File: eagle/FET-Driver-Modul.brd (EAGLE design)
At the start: 60 x 60 mm, 19 parts, among them X1 MKDSN1,5/3-5,08

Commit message: Lots of schema and board changes
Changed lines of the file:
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@@
 <wire x1="43.18" y1="52.07" x2="44.45" y2="54.61" width="1.016" layer="16"/>
 <contactref element="JP5" pad="1"/>
-<wire x1="25.4" y1="14.605" x2="26.67" y2="8.89" width="1.016" layer="16"/>
-<wire x1="26.67" y1="8.89" x2="34.29" y2="1.27" width="1.016" layer="16"/>
+<wire x1="25.4" y1="14.605" x2="25.4" y2="10.16" width="1.016" layer="16"/>
+<wire x1="25.4" y1="10.16" x2="34.29" y2="1.27" width="1.016" layer="16"/>
 <wire x1="34.29" y1="1.27" x2="47.625" y2="1.27" width="1.016" layer="16"/>
 <wire x1="47.625" y1="1.27" x2="49.53" y2="3.175" width="1.016" layer="16"/>

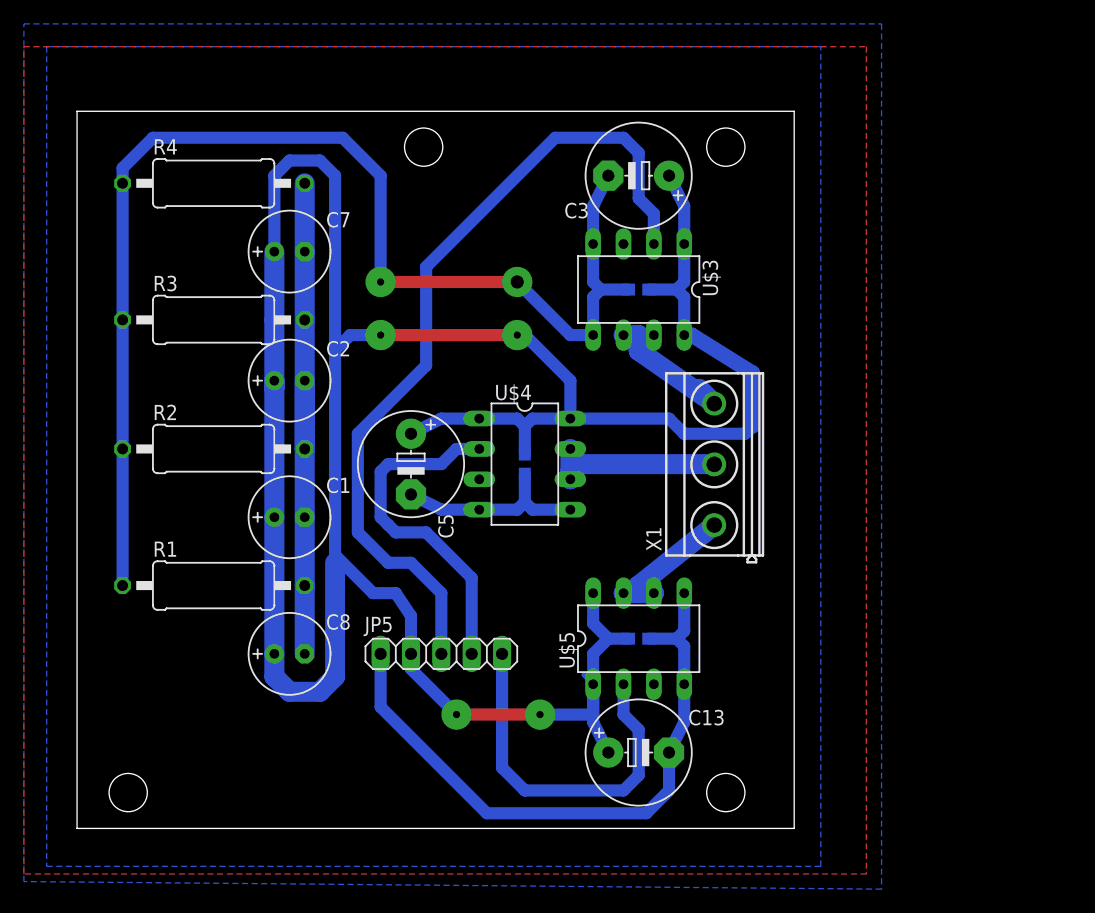
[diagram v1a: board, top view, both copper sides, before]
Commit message: Adjusted drill positions, little size corrections, new pin header
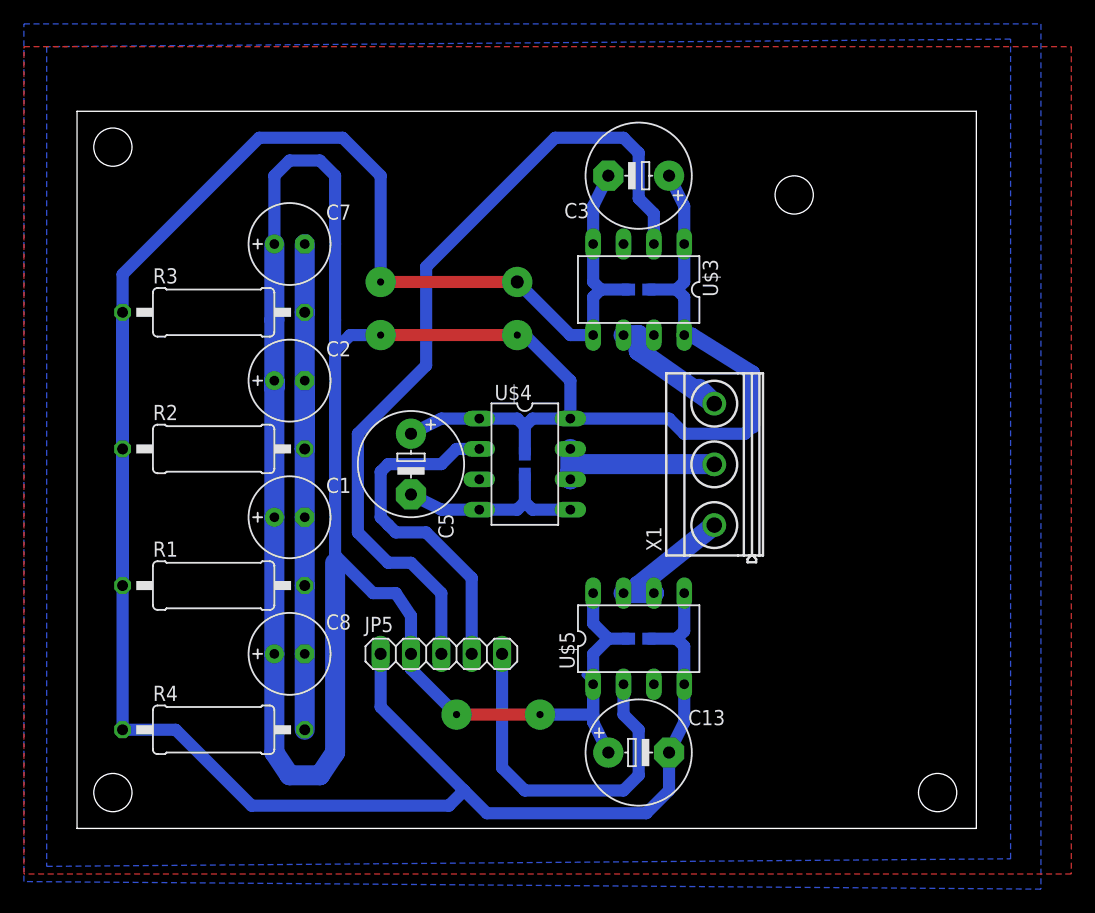
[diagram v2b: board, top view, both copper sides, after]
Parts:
- moved R4 45.7 mm to (11.4, 8.26)
- moved C7 0.64 mm to (17.8, 48.9)
- moved R3 0.63 mm to (11.4, 43.2)
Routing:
- net GND: track 156.6 -> 218.0 mm
- net N$2: track 231.7 -> 245.4 mm
- net N$4: track 50.8 -> 52.1 mm
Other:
- board size 60 x 60 mm -> 75.2 x 60 mm
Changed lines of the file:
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@@
 <board>
 <plain>
-<wire x1="0" y1="0" x2="60" y2="0" width="0" layer="20"/>
-<wire x1="60" y1="0" x2="60" y2="60" width="0" layer="20"/>
-<wire x1="60" y1="60" x2="0" y2="60" width="0" layer="20"/>
+<wire x1="0" y1="0" x2="75.24" y2="0" width="0" layer="20"/>
+<wire x1="75.24" y1="0" x2="75.24" y2="60" width="0" layer="20"/>
+<wire x1="75.24" y1="60" x2="0" y2="60" width="0" layer="20"/>
 <wire x1="0" y1="60" x2="0" y2="0" width="0" layer="20"/>
-<hole x="29" y="57" drill="3.2"/>
-<hole x="4.28" y="3" drill="3.2"/>
-<hole x="54.28" y="3" drill="3.2"/>
-<hole x="54.28" y="57" drill="3.2"/>
+<hole x="3" y="57" drill="3.2"/>
+<hole x="3" y="3" drill="3.2"/>
+<hole x="72" y="3" drill="3.2"/>
+<hole x="60" y="53" drill="3.2"/>
 </plain>
 <attributes>
@@
 <element name="C1" library="rcl" package="E2,5-7" value="100 µF" x="17.78" y="26.035"/>
 <element name="C2" library="rcl" package="E2,5-7" value="100 µF" x="17.78" y="37.465"/>
-<element name="C7" library="rcl" package="E2,5-7" value="100 µF" x="17.78" y="48.26"/>
+<element name="C7" library="rcl" package="E2,5-7" value="100 µF" x="17.78" y="48.895"/>
 <element name="C8" library="rcl" package="E2,5-7" value=" 100 µF" x="17.78" y="14.605"/>
 <element name="R1" library="resistor" package="0411/15" value="150" x="11.43" y="20.32"/>
 <element name="R2" library="resistor" package="0411/15" value="150" x="11.43" y="31.75"/>
-<element name="R3" library="resistor" package="0411/15" value="150" x="11.43" y="42.545"/>
-<element name="R4" library="resistor" package="0411/15" value="150" x="11.43" y="53.975"/>
+<element name="R3" library="resistor" package="0411/15" value="150" x="11.43" y="43.18"/>
+<element name="R4" library="resistor" package="0411/15" value="150" x="11.43" y="8.255"/>
 </elements>
 <signals>
@@
 <polygon width="0.4064" layer="16">
 <vertex x="-2.54" y="-3.175"/>
-<vertex x="62.23" y="-3.175"/>
-<vertex x="62.23" y="65.405"/>
+<vertex x="78.105" y="-2.54"/>
+<vertex x="78.105" y="66.04"/>
 <vertex x="-2.54" y="65.405"/>
 </polygon>
@@
 <contactref element="JP5" pad="1"/>
 <wire x1="25.4" y1="14.605" x2="25.4" y2="10.16" width="1.016" layer="16"/>
-<wire x1="25.4" y1="10.16" x2="34.29" y2="1.27" width="1.016" layer="16"/>
+<wire x1="25.4" y1="10.16" x2="32.385" y2="3.175" width="1.016" layer="16"/>
+<wire x1="32.385" y1="3.175" x2="34.29" y2="1.27" width="1.016" layer="16"/>
 <wire x1="34.29" y1="1.27" x2="47.625" y2="1.27" width="1.016" layer="16"/>
 <wire x1="47.625" y1="1.27" x2="49.53" y2="3.175" width="1.016" layer="16"/>
@@
 <contactref element="R3" pad="1"/>
 <contactref element="R2" pad="1"/>
-<wire x1="3.81" y1="53.975" x2="3.81" y2="42.545" width="1.016" layer="16"/>
+<wire x1="3.81" y1="8.255" x2="3.81" y2="43.18" width="1.016" layer="16"/>
 <wire x1="25.4" y1="45.72" x2="25.4" y2="54.61" width="1.016" layer="16"/>
 <wire x1="25.4" y1="54.61" x2="22.225" y2="57.785" width="1.016" layer="16"/>
-<wire x1="22.225" y1="57.785" x2="6.35" y2="57.785" width="1.016" layer="16"/>
-<wire x1="6.35" y1="57.785" x2="3.81" y2="55.245" width="1.016" layer="16"/>
-<wire x1="3.81" y1="55.245" x2="3.81" y2="53.975" width="1.016" layer="16"/>
-<wire x1="3.81" y1="42.545" x2="3.81" y2="31.75" width="1.016" layer="16"/>
+<wire x1="3.81" y1="43.18" x2="3.81" y2="31.75" width="1.016" layer="16"/>
 <wire x1="3.81" y1="20.32" x2="3.81" y2="31.75" width="1.016" layer="16"/>
 <polygon width="1.016" layer="1">
 <vertex x="-4.445" y="65.405"/>
-<vertex x="66.04" y="65.405"/>
-<vertex x="66.04" y="-3.81"/>
+<vertex x="83.185" y="65.405"/>
+<vertex x="83.185" y="-3.81"/>
 <vertex x="-4.445" y="-3.81"/>
 </polygon>
+<wire x1="22.225" y1="57.785" x2="15.24" y2="57.785" width="1.016" layer="16"/>
+<wire x1="15.24" y1="57.785" x2="3.81" y2="46.355" width="1.016" layer="16"/>
+<wire x1="3.81" y1="46.355" x2="3.81" y2="43.18" width="1.016" layer="16"/>
+<wire x1="3.81" y1="8.255" x2="8.255" y2="8.255" width="1.016" layer="16"/>
+<wire x1="8.255" y1="8.255" x2="14.605" y2="1.905" width="1.016" layer="16"/>
+<wire x1="14.605" y1="1.905" x2="31.115" y2="1.905" width="1.016" layer="16"/>
+<wire x1="31.115" y1="1.905" x2="32.385" y2="3.175" width="1.016" layer="16"/>
 </signal>
 <signal name="N$16">
 <polygon width="0.4064" layer="16">
 <vertex x="-4.445" y="67.31"/>
-<vertex x="67.31" y="67.31"/>
-<vertex x="67.31" y="-5.08"/>
+<vertex x="80.645" y="67.31"/>
+<vertex x="80.645" y="-5.08"/>
 <vertex x="-4.445" y="-4.445"/>
 </polygon>
@@
 <contactref element="C7" pad="+"/>
 <contactref element="C8" pad="+"/>
-<wire x1="16.51" y1="48.26" x2="16.51" y2="42.545" width="1.6764" layer="16"/>
+<wire x1="16.51" y1="48.895" x2="16.51" y2="42.545" width="1.6764" layer="16"/>
 <wire x1="16.51" y1="42.545" x2="16.51" y2="37.465" width="1.6764" layer="16"/>
 <wire x1="16.51" y1="37.465" x2="16.51" y2="36.83" width="1.6764" layer="16"/>
@@
 <wire x1="20.32" y1="55.88" x2="17.78" y2="55.88" width="1.016" layer="16"/>
 <wire x1="17.78" y1="55.88" x2="16.51" y2="54.61" width="1.016" layer="16"/>
-<wire x1="16.51" y1="54.61" x2="16.51" y2="48.26" width="1.016" layer="16"/>
+<wire x1="16.51" y1="54.61" x2="16.51" y2="48.895" width="1.016" layer="16"/>
 <wire x1="21.59" y1="42.545" x2="21.59" y2="48.895" width="1.016" layer="16"/>
 <wire x1="50.8" y1="41.275" x2="51.435" y2="41.275" width="1.27" layer="16"/>
 <wire x1="51.435" y1="41.275" x2="56.515" y2="38.1" width="1.27" layer="16"/>
 <wire x1="56.515" y1="38.1" x2="56.515" y2="33.655" width="1.27" layer="16"/>
-<wire x1="16.51" y1="14.605" x2="16.51" y2="12.7" width="1.6764" layer="16"/>
-<wire x1="16.51" y1="12.7" x2="17.78" y2="11.43" width="1.6764" layer="16"/>
-<wire x1="17.78" y1="11.43" x2="20.32" y2="11.43" width="1.6764" layer="16"/>
-<wire x1="20.32" y1="11.43" x2="21.59" y2="12.7" width="1.6764" layer="16"/>
-<wire x1="21.59" y1="12.7" x2="21.59" y2="22.225" width="1.6764" layer="16"/>
+<wire x1="16.51" y1="14.605" x2="16.51" y2="6.35" width="1.6764" layer="16"/>
+<wire x1="16.51" y1="6.35" x2="17.78" y2="4.445" width="1.6764" layer="16"/>
+<wire x1="17.78" y1="4.445" x2="20.32" y2="4.445" width="1.6764" layer="16"/>
+<wire x1="20.32" y1="4.445" x2="21.59" y2="6.35" width="1.6764" layer="16"/>
+<wire x1="21.59" y1="6.35" x2="21.59" y2="22.225" width="1.6764" layer="16"/>
 </signal>
 <signal name="N$1">
@@
 <contactref element="R4" pad="2"/>
 <wire x1="19.05" y1="31.75" x2="19.05" y2="37.465" width="1.6764" layer="16"/>
-<wire x1="19.05" y1="31.75" x2="19.05" y2="42.545" width="1.6764" layer="16"/>
-<wire x1="19.05" y1="53.975" x2="19.05" y2="48.26" width="1.6764" layer="16"/>
-<wire x1="19.05" y1="48.26" x2="19.05" y2="42.545" width="1.6764" layer="16"/>
+<wire x1="19.05" y1="31.75" x2="19.05" y2="43.18" width="1.6764" layer="16"/>
+<wire x1="19.05" y1="48.895" x2="19.05" y2="43.18" width="1.6764" layer="16"/>
 <wire x1="19.05" y1="20.32" x2="19.05" y2="26.035" width="1.016" layer="16"/>
+<wire x1="19.05" y1="8.255" x2="19.05" y2="14.605" width="1.6764" layer="16"/>
 </signal>
 <signal name="N$5">

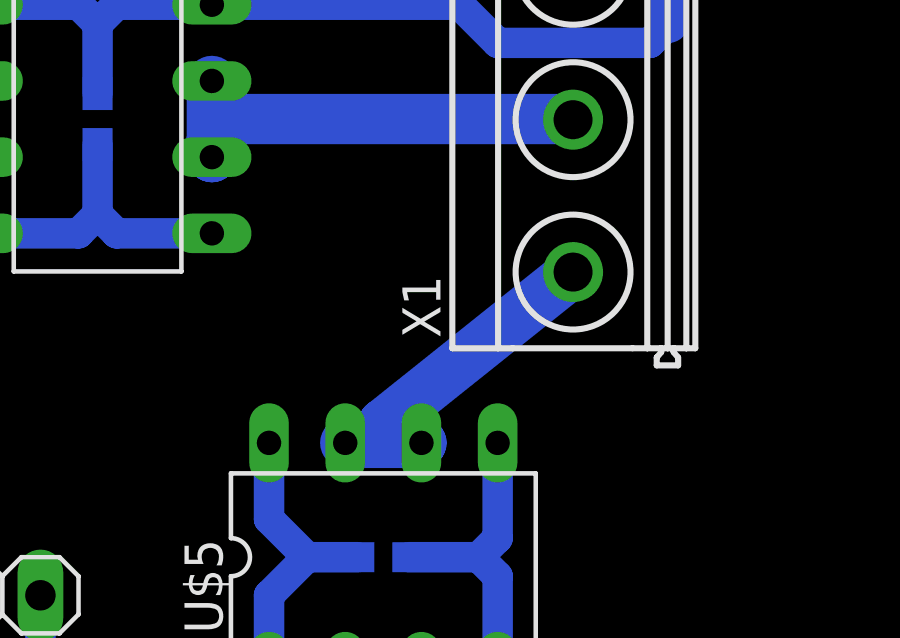
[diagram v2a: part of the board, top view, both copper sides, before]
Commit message: Minor documentation changes, reduced size of vsens Resistor to detect contact
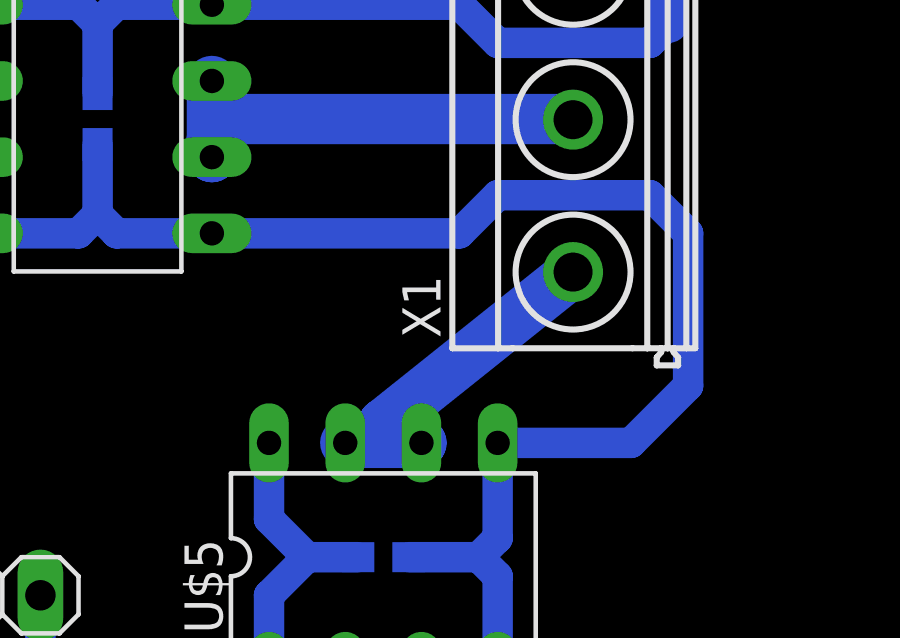
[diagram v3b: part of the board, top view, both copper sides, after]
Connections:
- removed net GND1: C5.-, C6.2, U$4.4, U$4.5
- net GND: now also C5.-, C6.2, U$4.4, U$4.5
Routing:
- net GND: track 218.0 -> 263.7 mm
- net GND1: track 16.5 -> 0.00 mm
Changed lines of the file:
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@@
 <wire x1="14.605" y1="1.905" x2="31.115" y2="1.905" width="1.016" layer="16"/>
 <wire x1="31.115" y1="1.905" x2="32.385" y2="3.175" width="1.016" layer="16"/>
+<contactref element="C5" pad="-"/>
+<contactref element="C6" pad="2"/>
+<contactref element="U$4" pad="5"/>
+<contactref element="U$4" pad="4"/>
+<wire x1="37.465" y1="29.63" x2="37.465" y2="27.305" width="1.016" layer="16"/>
+<wire x1="37.465" y1="27.305" x2="38.1" y2="26.67" width="1.016" layer="16"/>
+<wire x1="38.1" y1="26.67" x2="41.275" y2="26.67" width="1.016" layer="16"/>
+<wire x1="33.655" y1="26.67" x2="36.83" y2="26.67" width="1.016" layer="16"/>
+<wire x1="36.83" y1="26.67" x2="37.465" y2="27.305" width="1.016" layer="16"/>
+<wire x1="33.655" y1="26.67" x2="30.48" y2="26.67" width="1.016" layer="16"/>
+<wire x1="30.48" y1="26.67" x2="27.94" y2="27.94" width="1.016" layer="16"/>
+<wire x1="41.275" y1="26.67" x2="49.53" y2="26.67" width="1.016" layer="16"/>
+<wire x1="49.53" y1="26.67" x2="50.8" y2="27.94" width="1.016" layer="16"/>
+<wire x1="50.8" y1="27.94" x2="55.88" y2="27.94" width="1.016" layer="16"/>
+<wire x1="55.88" y1="27.94" x2="57.15" y2="26.67" width="1.016" layer="16"/>
+<wire x1="57.15" y1="26.67" x2="57.15" y2="21.59" width="1.016" layer="16"/>
+<wire x1="57.15" y1="21.59" x2="55.245" y2="19.685" width="1.016" layer="16"/>
+<wire x1="55.245" y1="19.685" x2="50.8" y2="19.685" width="1.016" layer="16"/>
 </signal>
 <signal name="N$16">
@@
 <wire x1="46.99" y1="20.3239" x2="53.315" y2="25.3789" width="1.6764" layer="16"/>
 </signal>
-<signal name="GND1">
-<contactref element="C5" pad="-"/>
-<contactref element="C6" pad="2"/>
-<contactref element="U$4" pad="5"/>
-<contactref element="U$4" pad="4"/>
-<wire x1="37.465" y1="29.63" x2="37.465" y2="27.305" width="1.016" layer="16"/>
-<wire x1="37.465" y1="27.305" x2="38.1" y2="26.67" width="1.016" layer="16"/>
-<wire x1="38.1" y1="26.67" x2="41.275" y2="26.67" width="1.016" layer="16"/>
-<wire x1="33.655" y1="26.67" x2="36.83" y2="26.67" width="1.016" layer="16"/>
-<wire x1="36.83" y1="26.67" x2="37.465" y2="27.305" width="1.016" layer="16"/>
-<wire x1="33.655" y1="26.67" x2="30.48" y2="26.67" width="1.016" layer="16"/>
-<wire x1="30.48" y1="26.67" x2="27.94" y2="27.94" width="1.016" layer="16"/>
-</signal>
 <signal name="N$2">
